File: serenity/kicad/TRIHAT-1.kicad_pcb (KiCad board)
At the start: 4 copper layers, 65 x 48 mm, 63 parts, among them J1 JST-GH-6P, J2 JST-GH-4P, J3 JST-GH-6P, J4 JST-GH-6P, J5 JST-GH-6P, J6 JST-GH-4P, J7 JST-GH-4P, J8 JST-GH-4P, U1 ICM-42688-P, U2 BMP388, U3 M10Q, U4 MCP2518FD, U5 MCP2562FD, U6 W5500, U7 HX1188NL, U8 SLB9670, U9 AP2112K-3.3, Y1 25MHz

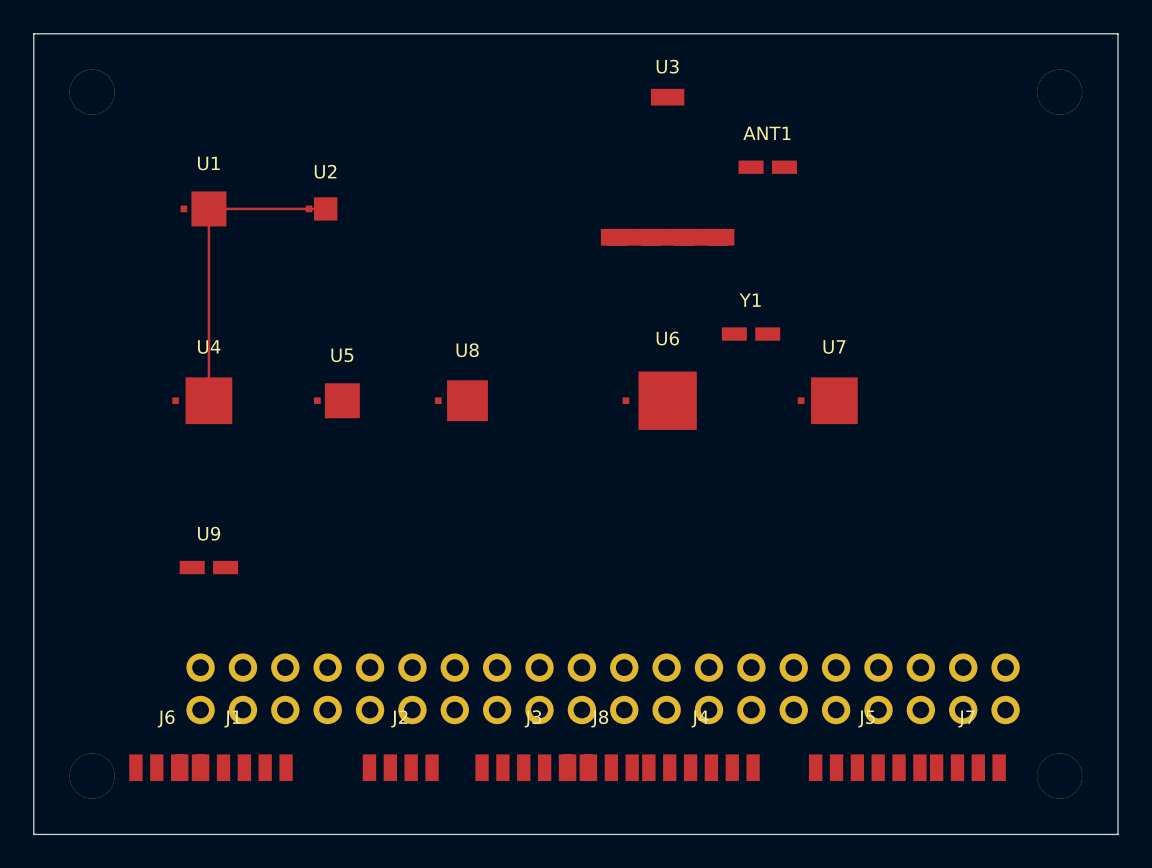
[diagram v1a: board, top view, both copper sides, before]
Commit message: Replace generic PCB silk labels with short descriptive names
Update all F.SilkS/B.SilkS fp_text reference labels across 7 KiCad PCB
files, replacing J/U/T numeric designators with function-based names so
each component is identifiable on the board without a BOM lookup.

CAPE-A-1 / CAPE-A-1-no-comment:
  J1→PB2-P1, J2→PB2-P2, U1→IMU, U2→BARO, U3→GPS,
  U4/U5→CAN-TR/RS485, U6→1553-DRV, U7→1553-RCV, T1→1553-XFM,
  U8/U9→ETH1-PHY/ETH2-PHY, U10→TPM,
  J3→CAN-FD, J4→RS-485, J5→MIL-1553, J6→ETH1, J7→ETH2,
  J8→ESC-TLM, J9→SERVO, J10→PWR-IN

CAPE-B-1 (adds RF + payload peripherals):
  U1→LORA, U2→WIFI-BT, U10→SD-WB, U11→NOR-FLASH,
  U12→WINCH-DRV, U13→LOAD-ADC, U14→PWM-I2C,
  J8→SIK-TLM, J9→RC-RCVR, J11→WINCH, J12→LOAD-CELL, J13→NAV-LIGHT

COMMS-HAT-1 (connectors + crystal only; ICs already descriptive):
  J1→SIK-UART, J2→ETH, J3→GPIO-EXT, J4→CAN-FD,
  JP4→PWR-IN, Y1→ETH-CLK

COMMS-HAT-SWITCH:
  Y1→SW-CLK

TRIHAT-1 (superseded; ICs + inferred connector mapping):
  U1→IMU, U2→BARO, U3→GPS, U4→CAN-CTRL, U5→CAN-TR,
  U6→ETH-CTRL, U7→ETH-MAG, U8→TPM, U9→LDO, Y1→ETH-CLK,
  J-connectors mapped from net list (GPS/CAN-FD/ETH/ESC-OUT/SERVO-OUT/etc.)

CM3-CARRIER-1:
  J1→CM3-SDIMM, U1→CAN-CTRL, U1B→CAN-TR, U2→RS485,
  U3→MIL-1553, U4→ETH-CTRL, U5→USB-UART, U6→LDO, U7→HAT-EEPROM

Boards already fully descriptive (SENSORHAT-1, CM4-CARRIER-1,
CM4-CARRIER-2) are unchanged.

https://claude.ai/code/session_01GniMw4QukTVM7JMzyVjH6p
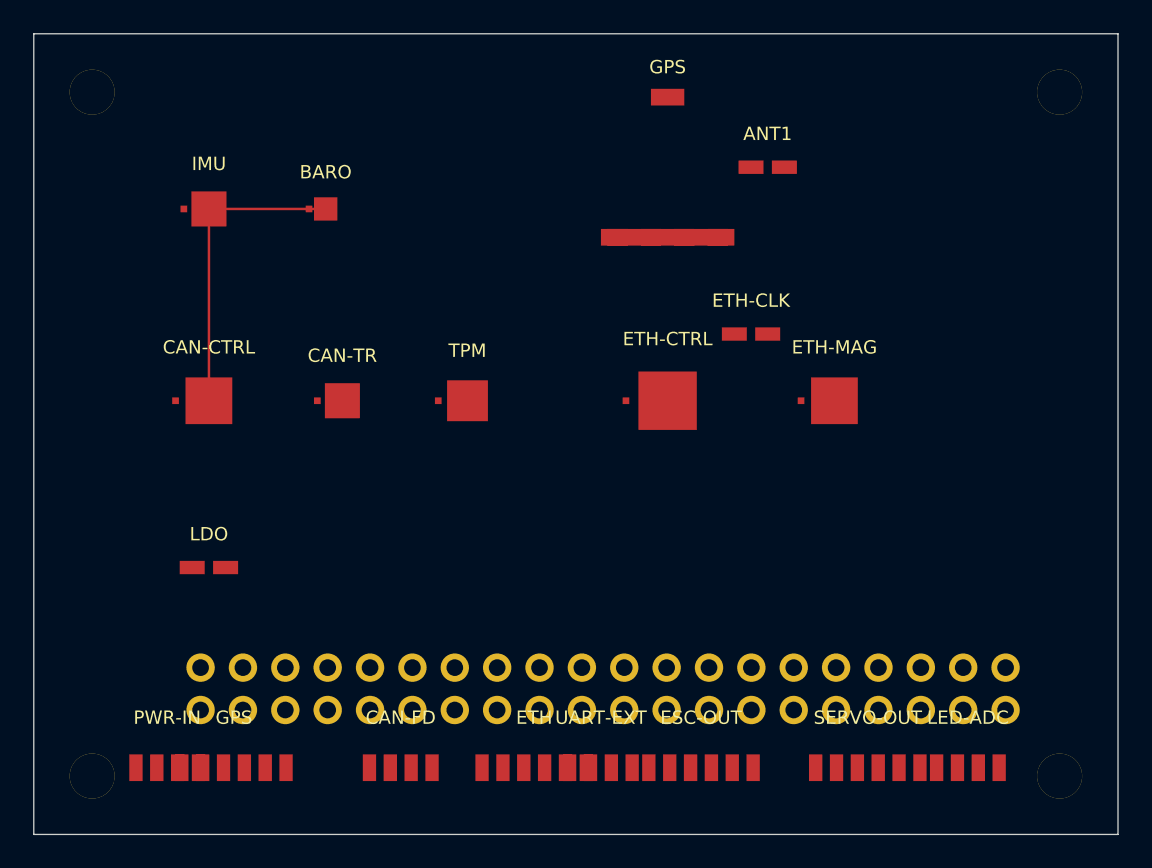
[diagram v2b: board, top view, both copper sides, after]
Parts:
- removed J1, J3, J4, J5: JST-GH-6P, Connector_JST:JST_GH_SM06B-GHS-TB_1x06_P1.25mm_Horizontal
- removed J2, J6, J7, J8: JST-GH-4P, Connector_JST:JST_GH_SM04B-GHS-TB_1x04_P1.25mm_Horizontal
- removed U1: ICM-42688-P, Package_DFN_QFN:QFN-30
- removed U2: BMP388, Package_DFN_QFN:QFN-20
- removed U3: M10Q, RF_GPS:u-blox_CAM-M8
- removed U4: MCP2518FD, Package_DFN_QFN:QFN-40
- removed U5: MCP2562FD, Package_DFN_QFN:QFN-30
- removed U6: W5500, Package_DFN_QFN:QFN-50
- removed U7: HX1188NL, Package_DFN_QFN:QFN-40
- removed U8: SLB9670, Package_DFN_QFN:QFN-35
- removed U9: AP2112K-3.3, Package_TO_SOT_SMD:SOT-23-5
- removed Y1: 25MHz, Crystal:Crystal_SMD_3225-4Pin_3.2x2.5mm
- added BARO: BMP388, Package_DFN_QFN:QFN-20, F.Cu at (17.5, 10.5)
- added CAN-CTRL: MCP2518FD, Package_DFN_QFN:QFN-40, F.Cu at (10.5, 22.0)
- added CAN-FD: JST-GH-4P, Connector_JST:JST_GH_SM04B-GHS-TB_1x04_P1.25mm_Horizontal, F.Cu at (22.0, 44.0)
- added CAN-TR: MCP2562FD, Package_DFN_QFN:QFN-30, F.Cu at (18.5, 22.0)
- added ESC-OUT: JST-GH-6P, Connector_JST:JST_GH_SM06B-GHS-TB_1x06_P1.25mm_Horizontal, F.Cu at (40.0, 44.0)
- added ETH: JST-GH-6P, Connector_JST:JST_GH_SM06B-GHS-TB_1x06_P1.25mm_Horizontal, F.Cu at (30.0, 44.0)
- added ETH-CLK: 25MHz, Crystal:Crystal_SMD_3225-4Pin_3.2x2.5mm, F.Cu at (43.0, 18.0)
- added ETH-CTRL: W5500, Package_DFN_QFN:QFN-50, F.Cu at (38.0, 22.0)
- added ETH-MAG: HX1188NL, Package_DFN_QFN:QFN-40, F.Cu at (48.0, 22.0)
- added GPS: M10Q, RF_GPS:u-blox_CAM-M8, F.Cu at (38.0, 8.00)
- added GPS: JST-GH-6P, Connector_JST:JST_GH_SM06B-GHS-TB_1x06_P1.25mm_Horizontal, F.Cu at (12.0, 44.0)
- added IMU: ICM-42688-P, Package_DFN_QFN:QFN-30, F.Cu at (10.5, 10.5)
- added LDO: AP2112K-3.3, Package_TO_SOT_SMD:SOT-23-5, F.Cu at (10.5, 32.0)
- added LED-ADC: JST-GH-4P, Connector_JST:JST_GH_SM04B-GHS-TB_1x04_P1.25mm_Horizontal, F.Cu at (56.0, 44.0)
- added PWR-IN: JST-GH-4P, Connector_JST:JST_GH_SM04B-GHS-TB_1x04_P1.25mm_Horizontal, F.Cu at (8.00, 44.0)
- added SERVO-OUT: JST-GH-6P, Connector_JST:JST_GH_SM06B-GHS-TB_1x06_P1.25mm_Horizontal, F.Cu at (50.0, 44.0)
- added TPM: SLB9670, Package_DFN_QFN:QFN-35, F.Cu at (26.0, 22.0)
- added UART-EXT: JST-GH-4P, Connector_JST:JST_GH_SM04B-GHS-TB_1x04_P1.25mm_Horizontal, F.Cu at (34.0, 44.0)
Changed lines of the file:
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@@
     (at 10.5 10.5)
     (property "Description" "6-DOF IMU SPI0 24MHz LGA-14")
-    (fp_text reference "U1" (at 0 -2.7) (layer "F.SilkS")
+    (fp_text reference "IMU" (at 0 -2.7) (layer "F.SilkS")
       (effects (font (size 0.8 0.8) (thickness 0.15))))
     (fp_text value "ICM-42688-P" (at 0 2.7) (layer "F.Fab")
@@
     (at 17.5 10.5)
     (property "Description" "Barometer I2C1 LGA-8")
-    (fp_text reference "U2" (at 0 -2.2) (layer "F.SilkS")
+    (fp_text reference "BARO" (at 0 -2.2) (layer "F.SilkS")
       (effects (font (size 0.8 0.8) (thickness 0.15))))
     (fp_text value "BMP388" (at 0 2.2) (layer "F.Fab")
@@
   (footprint "RF_GPS:u-blox_CAM-M8" (layer "F.Cu")
     (at 38 8) (property "Description" "u-blox M10Q GPS module")
-    (fp_text reference "U3" (at 0 -6) (layer "F.SilkS")
+    (fp_text reference "GPS" (at 0 -6) (layer "F.SilkS")
       (effects (font (size 0.8 0.8) (thickness 0.15))))
     (fp_text value "M10Q" (at 0 6) (layer "F.Fab")
@@
     (at 10.5 22)
     (property "Description" "CAN FD controller SOIC-20 SPI0")
-    (fp_text reference "U4" (at 0 -3.2) (layer "F.SilkS")
+    (fp_text reference "CAN-CTRL" (at 0 -3.2) (layer "F.SilkS")
       (effects (font (size 0.8 0.8) (thickness 0.15))))
     (fp_text value "MCP2518FD" (at 0 3.2) (layer "F.Fab")
@@
     (at 18.5 22)
     (property "Description" "CAN FD transceiver SOIC-8")
-    (fp_text reference "U5" (at 0 -2.7) (layer "F.SilkS")
+    (fp_text reference "CAN-TR" (at 0 -2.7) (layer "F.SilkS")
       (effects (font (size 0.8 0.8) (thickness 0.15))))
     (fp_text value "MCP2562FD" (at 0 2.7) (layer "F.Fab")
@@
     (at 38 22)
     (property "Description" "Ethernet SPI controller LQFP-48")
-    (fp_text reference "U6" (at 0 -3.7) (layer "F.SilkS")
+    (fp_text reference "ETH-CTRL" (at 0 -3.7) (layer "F.SilkS")
       (effects (font (size 0.8 0.8) (thickness 0.15))))
     (fp_text value "W5500" (at 0 3.7) (layer "F.Fab")
@@
     (at 48 22)
     (property "Description" "Ethernet magnetics transformer")
-    (fp_text reference "U7" (at 0 -3.2) (layer "F.SilkS")
+    (fp_text reference "ETH-MAG" (at 0 -3.2) (layer "F.SilkS")
       (effects (font (size 0.8 0.8) (thickness 0.15))))
     (fp_text value "HX1188NL" (at 0 3.2) (layer "F.Fab")
@@
     (at 26 22)
     (property "Description" "TPM 2.0 SPI SOP-8")
-    (fp_text reference "U8" (at 0 -3.0) (layer "F.SilkS")
+    (fp_text reference "TPM" (at 0 -3.0) (layer "F.SilkS")
       (effects (font (size 0.8 0.8) (thickness 0.15))))
     (fp_text value "SLB9670" (at 0 3.0) (layer "F.Fab")
@@
     (at 10.5 32)
     (property "Description" "3.3V LDO 600mA ultra-low noise")
-    (fp_text reference "U9" (at 0 -2) (layer "F.SilkS")
+    (fp_text reference "LDO" (at 0 -2) (layer "F.SilkS")
       (effects (font (size 0.8 0.8) (thickness 0.15))))
     (fp_text value "AP2112K-3.3" (at 0 2) (layer "F.Fab")
@@
     (at 43 18)
     (property "Description" "W5500 reference clock")
-    (fp_text reference "Y1" (at 0 -2) (layer "F.SilkS")
+    (fp_text reference "ETH-CLK" (at 0 -2) (layer "F.SilkS")
       (effects (font (size 0.8 0.8) (thickness 0.15))))
     (fp_text value "25MHz" (at 0 2) (layer "F.Fab")
@@
   (footprint "Connector_JST:JST_GH_SM06B-GHS-TB_1x06_P1.25mm_Horizontal" (layer "F.Cu")
     (at 12 44) (property "Description" "JST-GH 1.25mm 6-pin connector")
-    (fp_text reference "J1" (at 0 -3) (layer "F.SilkS")
+    (fp_text reference "GPS" (at 0 -3) (layer "F.SilkS")
       (effects (font (size 0.8 0.8) (thickness 0.15))))
     (fp_text value "JST-GH-6P" (at 0 3) (layer "F.Fab")
@@
   (footprint "Connector_JST:JST_GH_SM04B-GHS-TB_1x04_P1.25mm_Horizontal" (layer "F.Cu")
     (at 22 44) (property "Description" "JST-GH 1.25mm 4-pin connector")
-    (fp_text reference "J2" (at 0 -3) (layer "F.SilkS")
+    (fp_text reference "CAN-FD" (at 0 -3) (layer "F.SilkS")
       (effects (font (size 0.8 0.8) (thickness 0.15))))
     (fp_text value "JST-GH-4P" (at 0 3) (layer "F.Fab")
@@
   (footprint "Connector_JST:JST_GH_SM06B-GHS-TB_1x06_P1.25mm_Horizontal" (layer "F.Cu")
     (at 30 44) (property "Description" "JST-GH 1.25mm 6-pin connector")
-    (fp_text reference "J3" (at 0 -3) (layer "F.SilkS")
+    (fp_text reference "ETH" (at 0 -3) (layer "F.SilkS")
       (effects (font (size 0.8 0.8) (thickness 0.15))))
     (fp_text value "JST-GH-6P" (at 0 3) (layer "F.Fab")
@@
   (footprint "Connector_JST:JST_GH_SM06B-GHS-TB_1x06_P1.25mm_Horizontal" (layer "F.Cu")
     (at 40 44) (property "Description" "JST-GH 1.25mm 6-pin connector")
-    (fp_text reference "J4" (at 0 -3) (layer "F.SilkS")
+    (fp_text reference "ESC-OUT" (at 0 -3) (layer "F.SilkS")
       (effects (font (size 0.8 0.8) (thickness 0.15))))
     (fp_text value "JST-GH-6P" (at 0 3) (layer "F.Fab")
@@
   (footprint "Connector_JST:JST_GH_SM06B-GHS-TB_1x06_P1.25mm_Horizontal" (layer "F.Cu")
     (at 50 44) (property "Description" "JST-GH 1.25mm 6-pin connector")
-    (fp_text reference "J5" (at 0 -3) (layer "F.SilkS")
+    (fp_text reference "SERVO-OUT" (at 0 -3) (layer "F.SilkS")
       (effects (font (size 0.8 0.8) (thickness 0.15))))
     (fp_text value "JST-GH-6P" (at 0 3) (layer "F.Fab")
@@
   (footprint "Connector_JST:JST_GH_SM04B-GHS-TB_1x04_P1.25mm_Horizontal" (layer "F.Cu")
     (at 8 44) (property "Description" "JST-GH 1.25mm 4-pin connector")
-    (fp_text reference "J6" (at 0 -3) (layer "F.SilkS")
+    (fp_text reference "PWR-IN" (at 0 -3) (layer "F.SilkS")
       (effects (font (size 0.8 0.8) (thickness 0.15))))
     (fp_text value "JST-GH-4P" (at 0 3) (layer "F.Fab")
@@
   (footprint "Connector_JST:JST_GH_SM04B-GHS-TB_1x04_P1.25mm_Horizontal" (layer "F.Cu")
     (at 56 44) (property "Description" "JST-GH 1.25mm 4-pin connector")
-    (fp_text reference "J7" (at 0 -3) (layer "F.SilkS")
+    (fp_text reference "LED-ADC" (at 0 -3) (layer "F.SilkS")
       (effects (font (size 0.8 0.8) (thickness 0.15))))
     (fp_text value "JST-GH-4P" (at 0 3) (layer "F.Fab")
@@
   (footprint "Connector_JST:JST_GH_SM04B-GHS-TB_1x04_P1.25mm_Horizontal" (layer "F.Cu")
     (at 34 44) (property "Description" "JST-GH 1.25mm 4-pin connector")
-    (fp_text reference "J8" (at 0 -3) (layer "F.SilkS")
-      (effects (font (size 0.8 0.8) (thickness 0.15))))
-    (fp_text value "JST-GH-4P" (at 0 3) (layer "F.Fab")
+    (fp_text reference "UART-EXT" (at 0 -3) (layer "F.SilkS")
+      (effects (font (size 0.8 0.8) (thickness 0.15))))
+    (fp_text value "JST-GH-4P" (at 0 3) (layer "F.Fab")
